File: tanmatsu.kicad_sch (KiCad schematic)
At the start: 47 parts, among them J1 USB host, J10 External Add-On (SAO / PMOD), J2 Micro_SD_Card, J3 USB device, J4 Headphone, J5 Speaker, J6 CAMERA, J7 SAO, J8 Expansion I3C, J9 Internal Add-On, SW1 Boot, U1 USBLC6-2P6, U2 CH334R, U3 TPD4E05U06DQAR, U4 USBLC6-2P6, U5 ESD, U6 ESD, Y1 12MHz

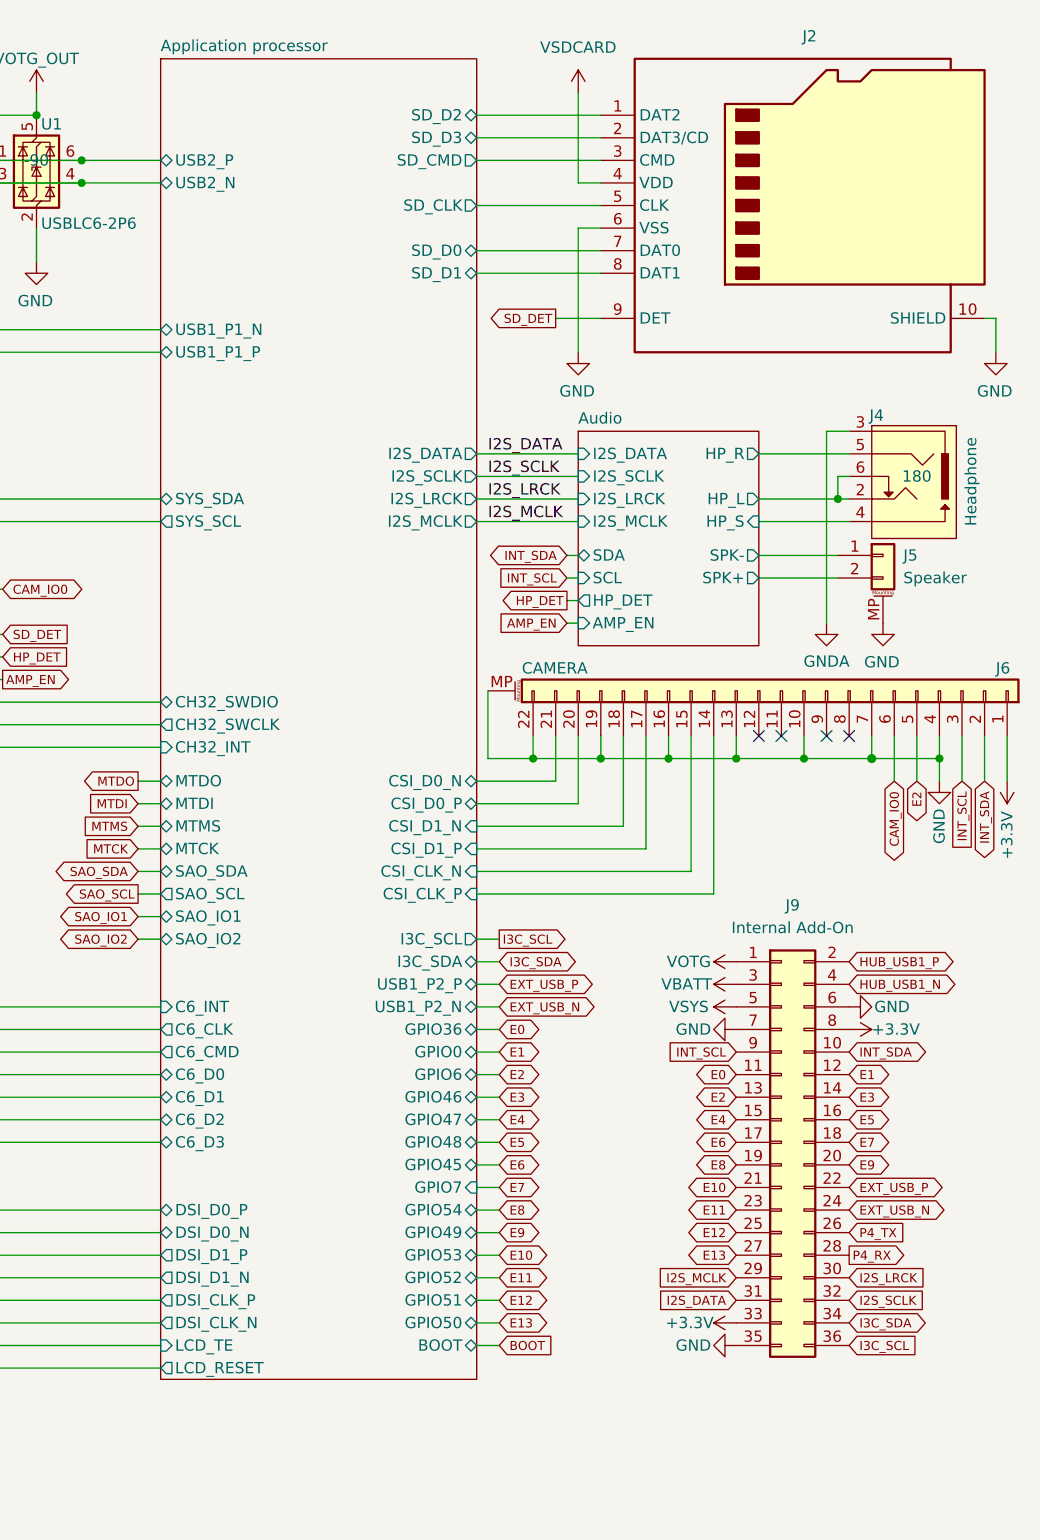
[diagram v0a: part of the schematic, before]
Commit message: Rev 6 (#17)
* Change SD card power circuit, change LCSC part for L1, change camera connector

* Enable IR LED for assembly, hide unwanted fields of P4 on schematic
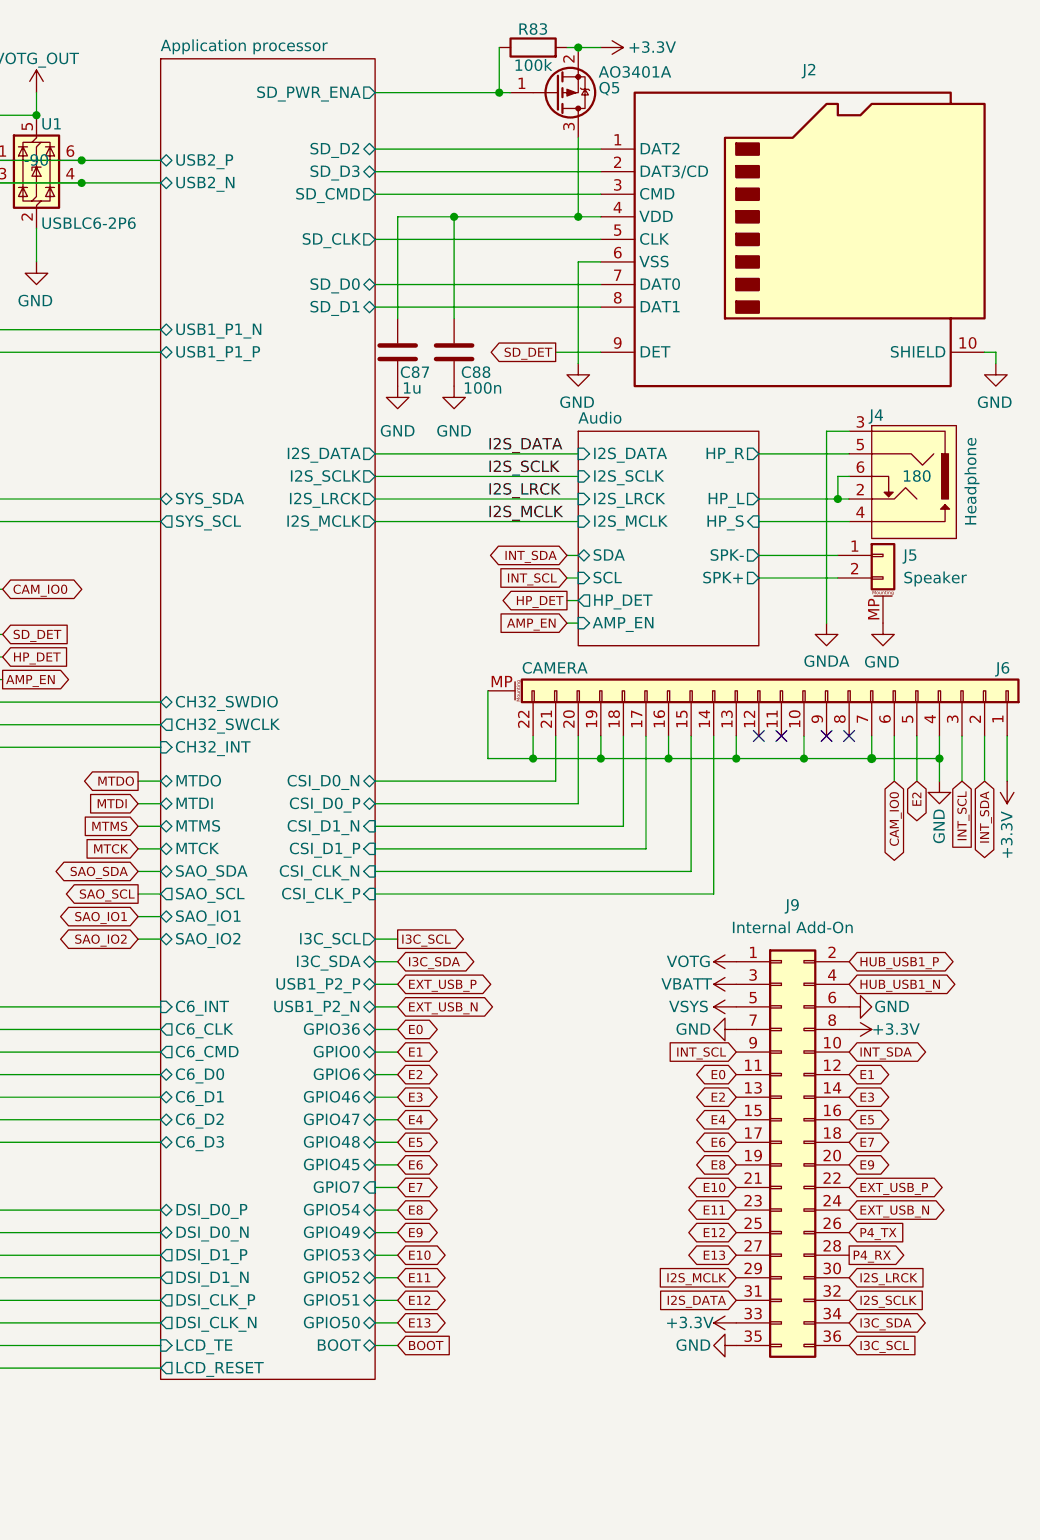
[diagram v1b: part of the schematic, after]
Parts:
- added C87: 1u, Capacitor_SMD:C_0603_1608Metric, symbol mch2021-rescue:C-Device
- added C88: 100n, Capacitor_SMD:C_0402_1005Metric, symbol symbols:C
- added Q5: AO3401A, Package_TO_SOT_SMD:SOT-23, symbol Transistor_FET:AO3401A
- added R83: 100k, Resistor_SMD:R_0402_1005Metric, symbol Device:R
- J6: footprint Connector_FFC-FPC:Hirose_FH12-22S-0.5SH_1x22-1MP_P0.50mm_Horizontal -> library:FPC-SMD_XUNPU_FPC-0.5FX-22PWBH20; LCSC C597981 -> C3446014
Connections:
- net +3.3V: now also Q5.2 (S), R83.2
- net GND: now also C87.2, C88.2
- net VSDCARD: no longer names the net of J2.4 (VDD)
- net VSDCARD: now also C87.1, C88.1, Q5.3 (D)
- new net Application processor/SD_PWR_ENA: Q5.1 (G), R83.1
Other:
- sheet Application processor ports: added SD_PWR_ENA; removed none
- moved on the sheet: J2

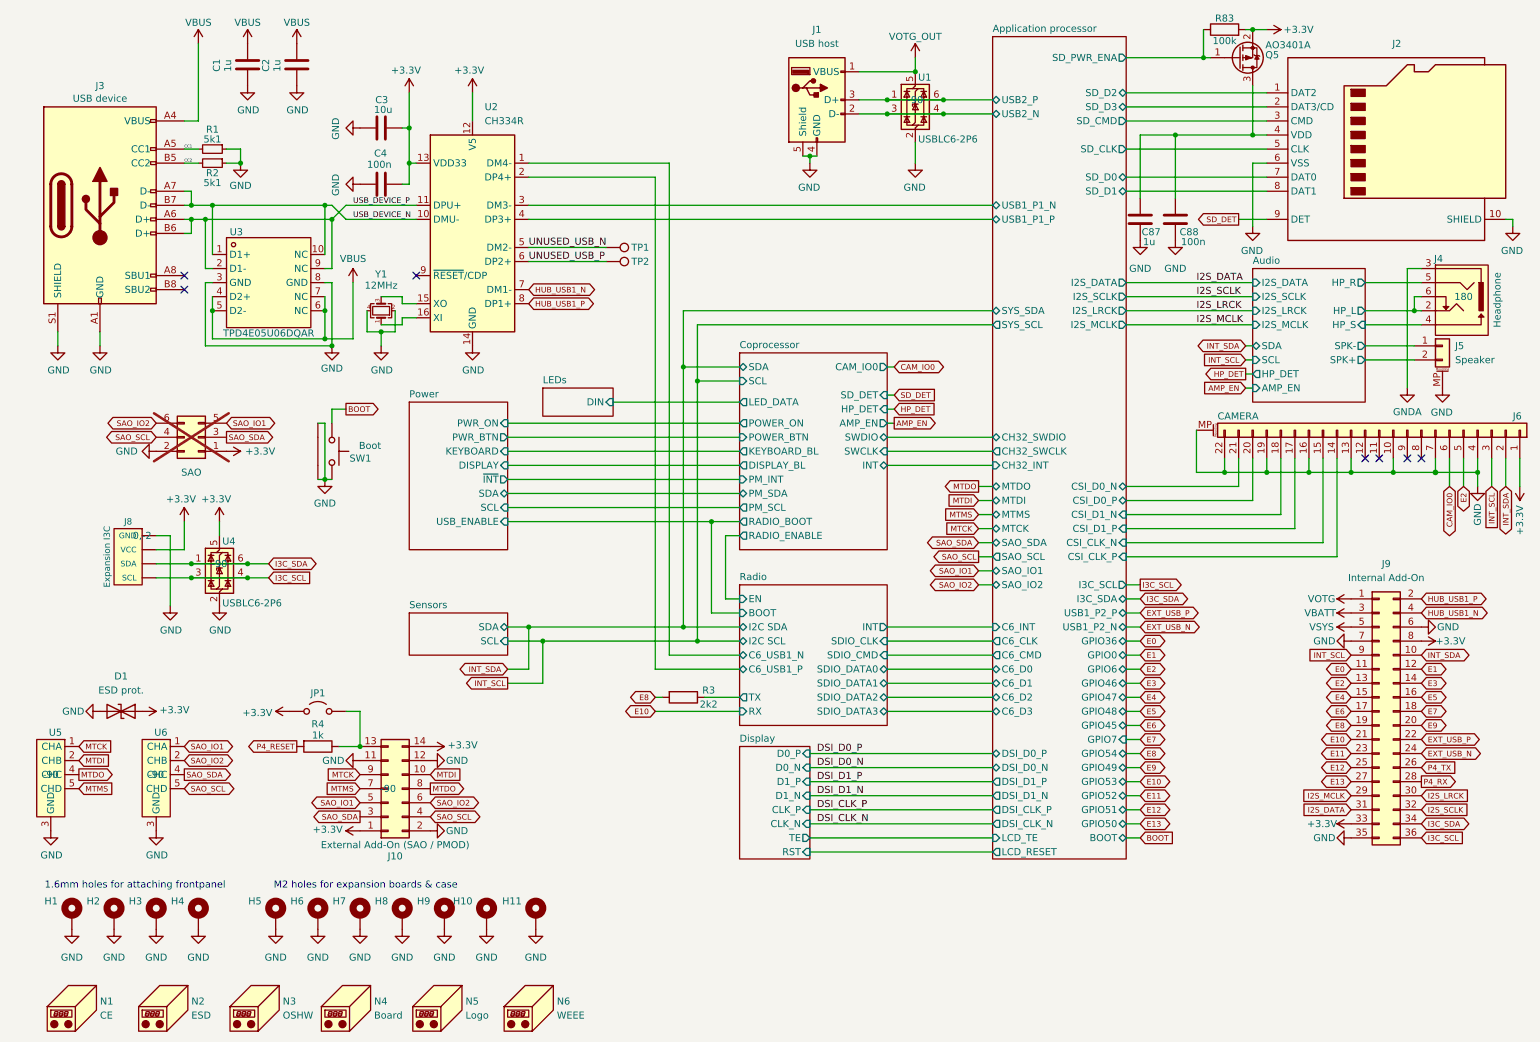
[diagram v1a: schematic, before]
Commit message: Revision 7 (#18)
* Revision 7: fix SD card power control circuit

* Add missing LCSC SKU
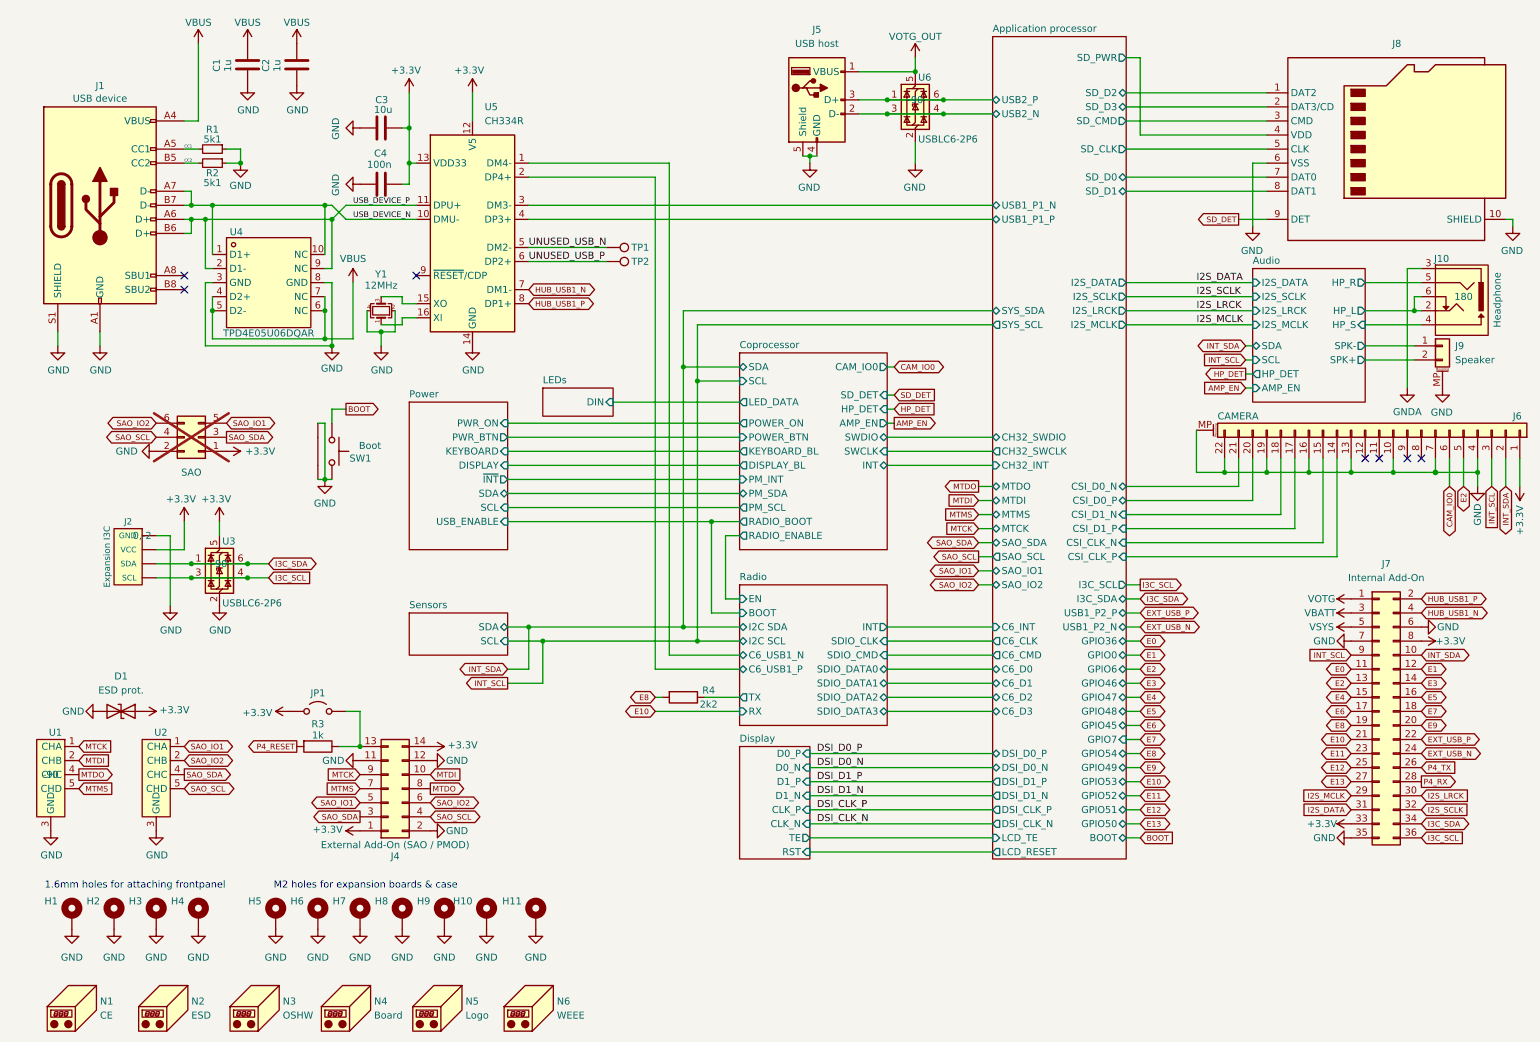
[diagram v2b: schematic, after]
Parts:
- removed C87: 1u, Capacitor_SMD:C_0603_1608Metric, symbol mch2021-rescue:C-Device
- removed C88: 100n, Capacitor_SMD:C_0402_1005Metric, symbol symbols:C
- removed Q5: AO3401A, Package_TO_SOT_SMD:SOT-23, symbol Transistor_FET:AO3401A
- removed R83: 100k, Resistor_SMD:R_0402_1005Metric, symbol Device:R
- renumbered J3 to J1, J4 to J10, J8 to J2, J7 to J3, J10 to J4, J1 to J5, J9 to J7, J2 to J8, J5 to J9, R4 to R3, R3 to R4, U5 to U1, U6 to U2, U4 to U3, U3 to U4, U2 to U5, U1 to U6
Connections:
- net Application processor/SD_PWR: now reaches J8.4 (VDD)
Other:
- sheet Application processor ports: added SD_PWR; removed SD_PWR_ENA
